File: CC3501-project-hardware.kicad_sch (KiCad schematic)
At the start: 19 parts, among them J1 USB_C_Receptacle_USB2.0_16P, J2 Conn_01x02, U1 RP2040, U2 AMS1117-3.3, U3 CR2013-MI2120, U4 DS18B20, U5 DS18B20, U6 DS18B20, U7 HX711, U8 W25Q128JVSIQTR

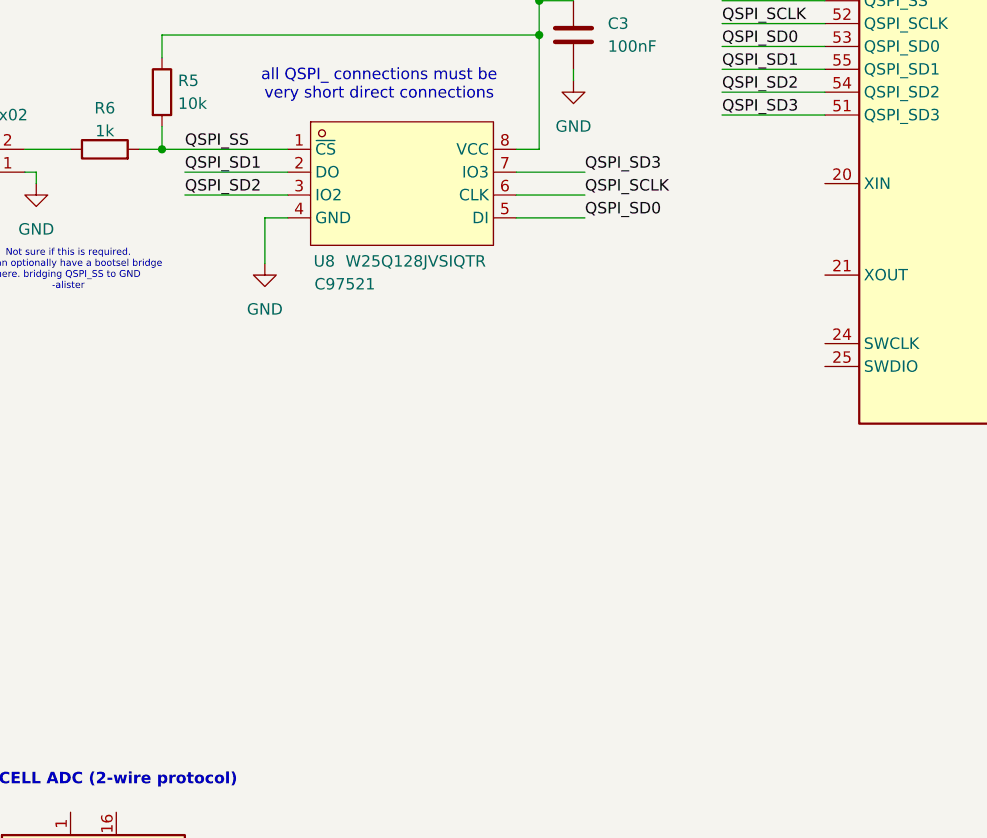
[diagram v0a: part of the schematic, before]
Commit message: Clock added
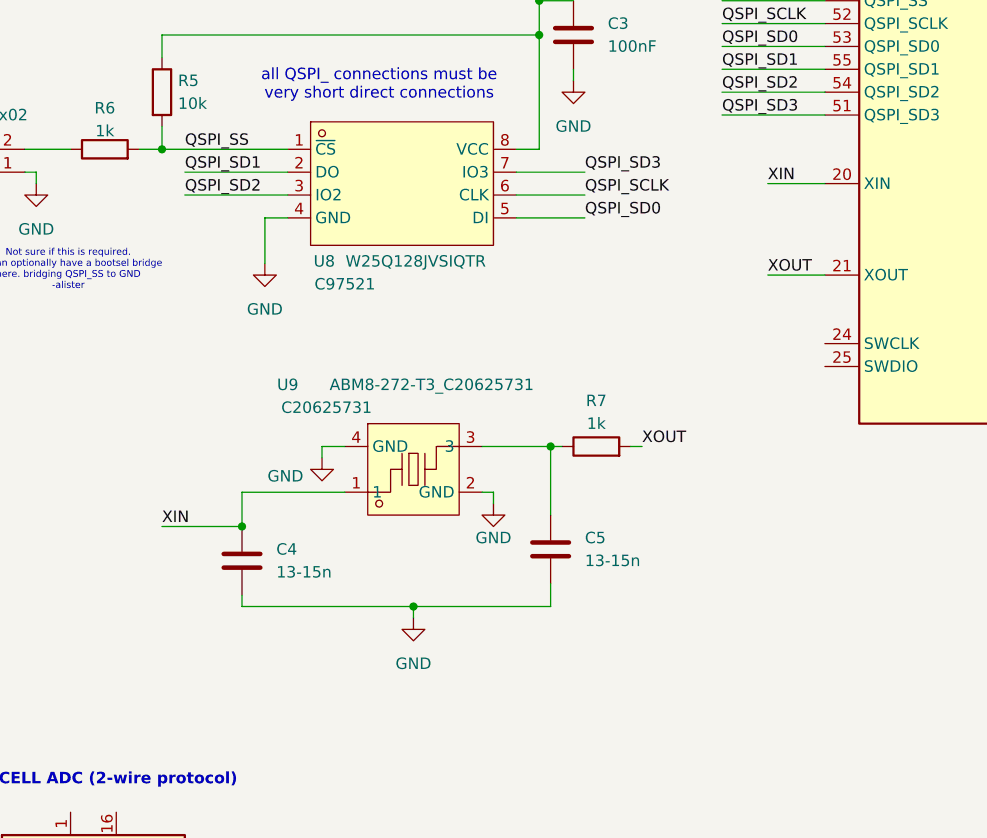
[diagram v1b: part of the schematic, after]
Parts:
- added C4, C5: 13-15n, symbol Device:C
- added R7: 1k, symbol Device:R
- added U9: ABM8-272-T3_C20625731, lcsc:CRYSTAL-SMD_4P-L3.2-W2.5-BL, symbol lcsc:ABM8-272-T3_C20625731
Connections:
- net GND: now also C4.2, C5.2, U9.2 (GND), U9.4 (GND)
- net XIN: now reaches U1.20 (XIN)
- net XIN: now also C4.1, U9.1
- net XOUT: now reaches U1.21 (XOUT)
- net XOUT: now also R7.2
- new net: C5.1, R7.1, U9.3

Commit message: Added a seperate page for rp2040 required parts
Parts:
- removed C3: 100nF, symbol Device:C
- removed C4, C5: 13-15n, symbol Device:C
- removed J2: Conn_01x02, symbol Connector_Generic:Conn_01x02
- removed R5: 10k, symbol Device:R
- removed R6, R7: 1k, symbol Device:R
- removed U8: W25Q128JVSIQTR, lcsc:SOIC-8_L5.3-W5.3-P1.27-LS8.0-BL, symbol lcsc:W25Q128JVSIQTR
- removed U9: ABM8-272-T3_C20625731, lcsc:CRYSTAL-SMD_4P-L3.2-W2.5-BL, symbol lcsc:ABM8-272-T3_C20625731
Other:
- added sheet rp2040stuff (untitled.kicad_sch)
- note removed: "Not sure if this is required. we can optionally have a bootsel bridge here. bridging QSPI_SS to GND -alister"
- note removed: "all QSPI_ connections must be very short direct connections"

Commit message: Renamed page 2
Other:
- sheet rp2040stuff renamed rp2040 components
- sheet rp2040 components: file untitled.kicad_sch -> rp2040components.kicad_sch
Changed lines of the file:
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@@
 			(color 0 0 0 0)
 		)
-		(property "Sheetname" "rp2040stuff"
+		(property "Sheetname" "rp2040 components"
 			(at 332.74 1.8284 0)
 			(show_name no)
@@
 			)
 		)
-		(property "Sheetfile" "untitled.kicad_sch"
+		(property "Sheetfile" "rp2040components.kicad_sch"
 			(at 332.74 211.4046 0)
 			(show_name no)

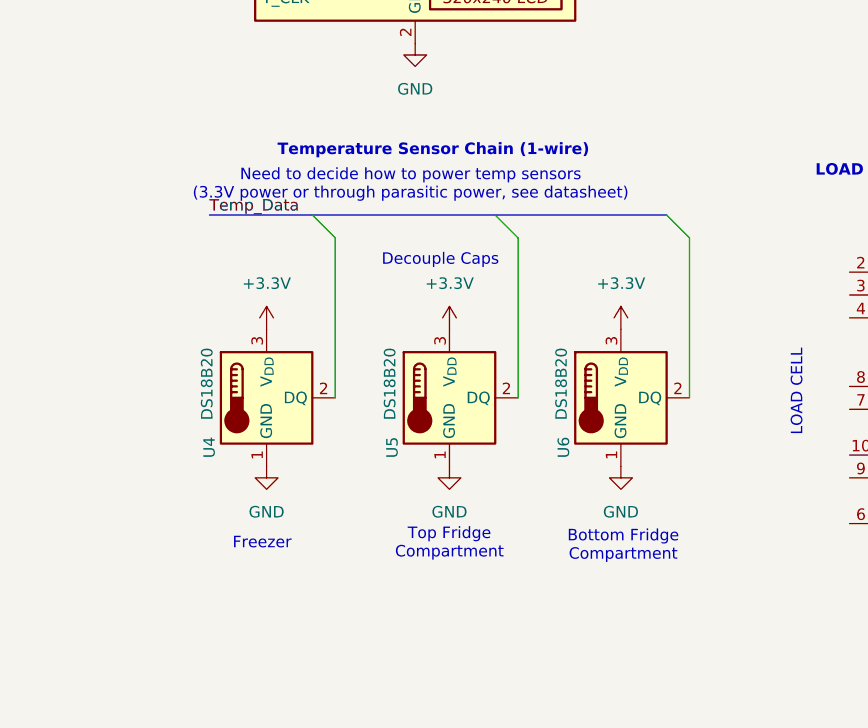
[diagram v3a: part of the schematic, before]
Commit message: Move DS18B20 breakout board into schematic.
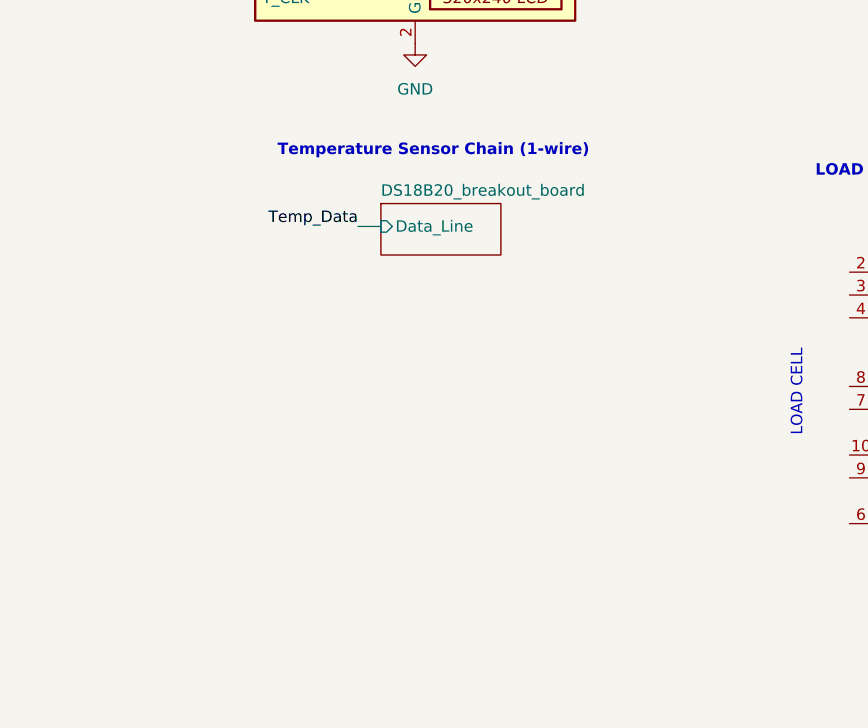
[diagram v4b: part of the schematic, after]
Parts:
- removed U4, U5, U6: DS18B20, Package_TO_SOT_THT:TO-92_Inline, symbol Sensor_Temperature:DS18B20
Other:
- added sheet DS18B20_breakout_board (DS18B20_breakout_board\DS18B20_breakout_board.kicad_sch)
- note removed: "Bottom Fridge Compartment"
- note removed: "Freezer"
- note removed: "Need to decide how to power temp sensors (3.3V power or through parasitic power, see datasheet)"
- note removed: "Top Fridge Compartment"

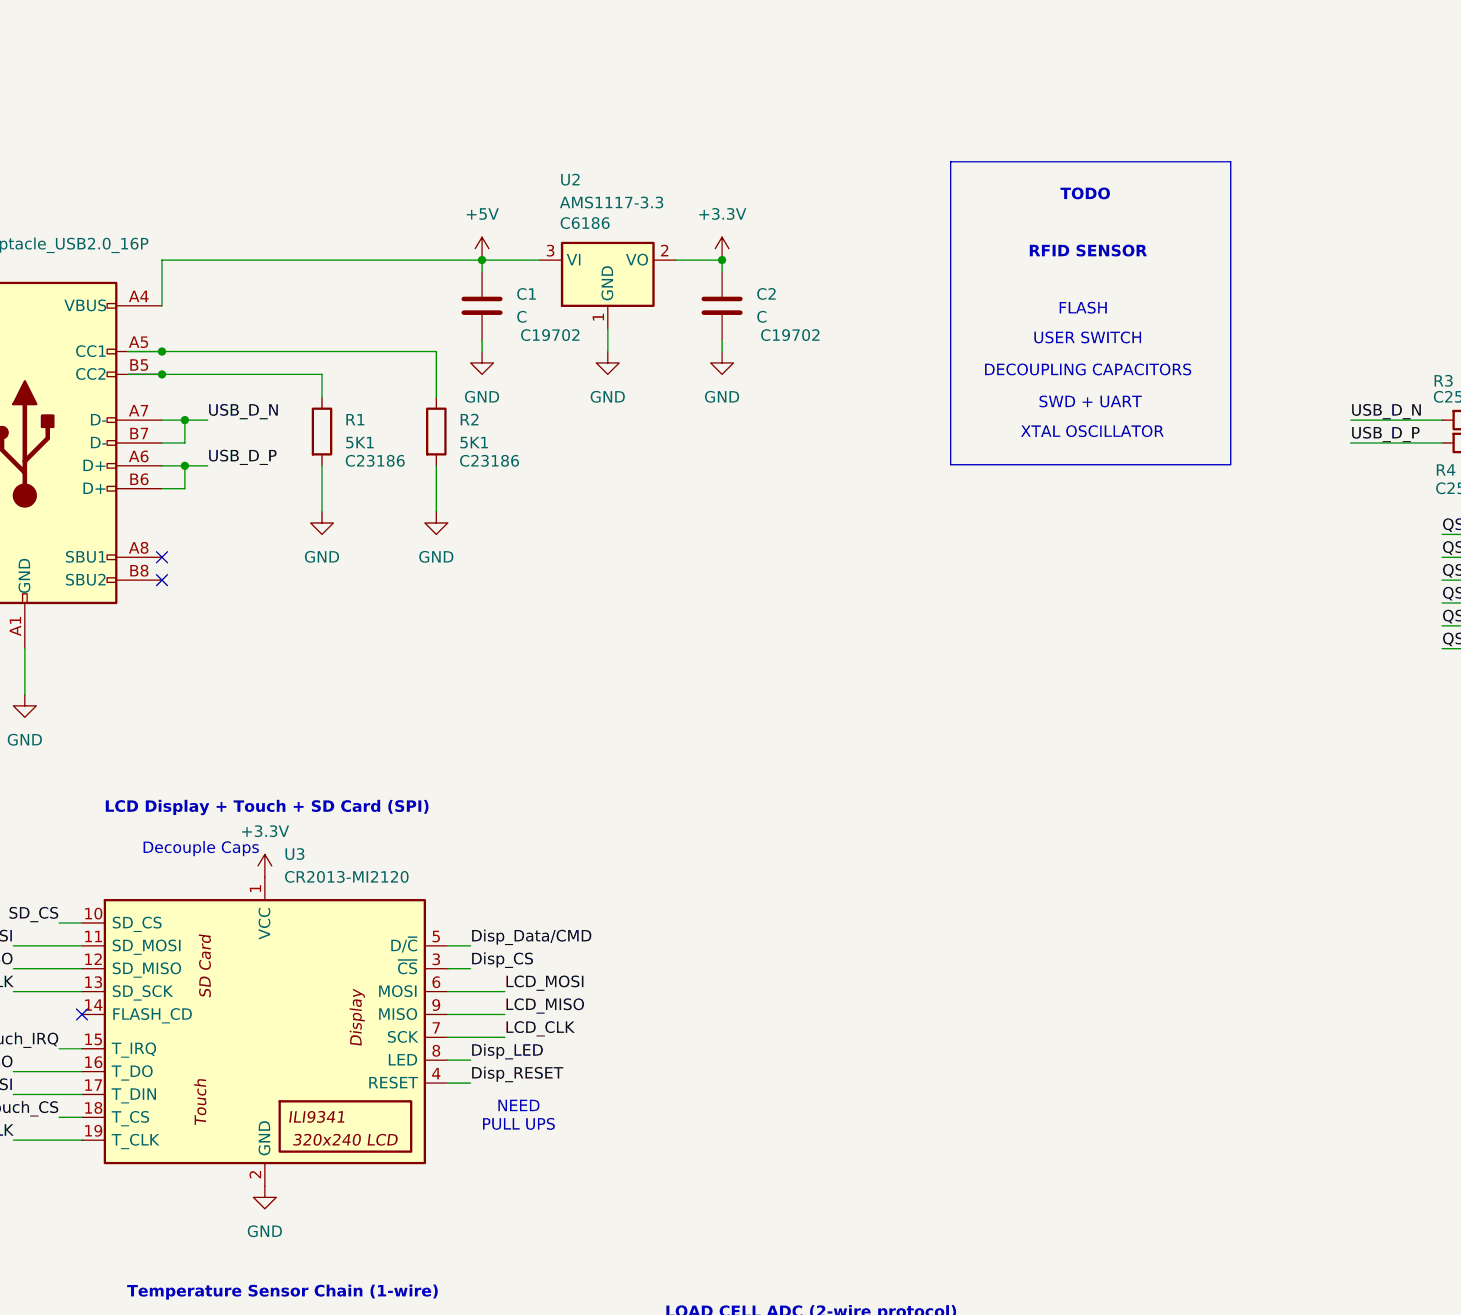
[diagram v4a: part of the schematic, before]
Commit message: add new dc-dc converter with recommended circuit layout for 3.3v
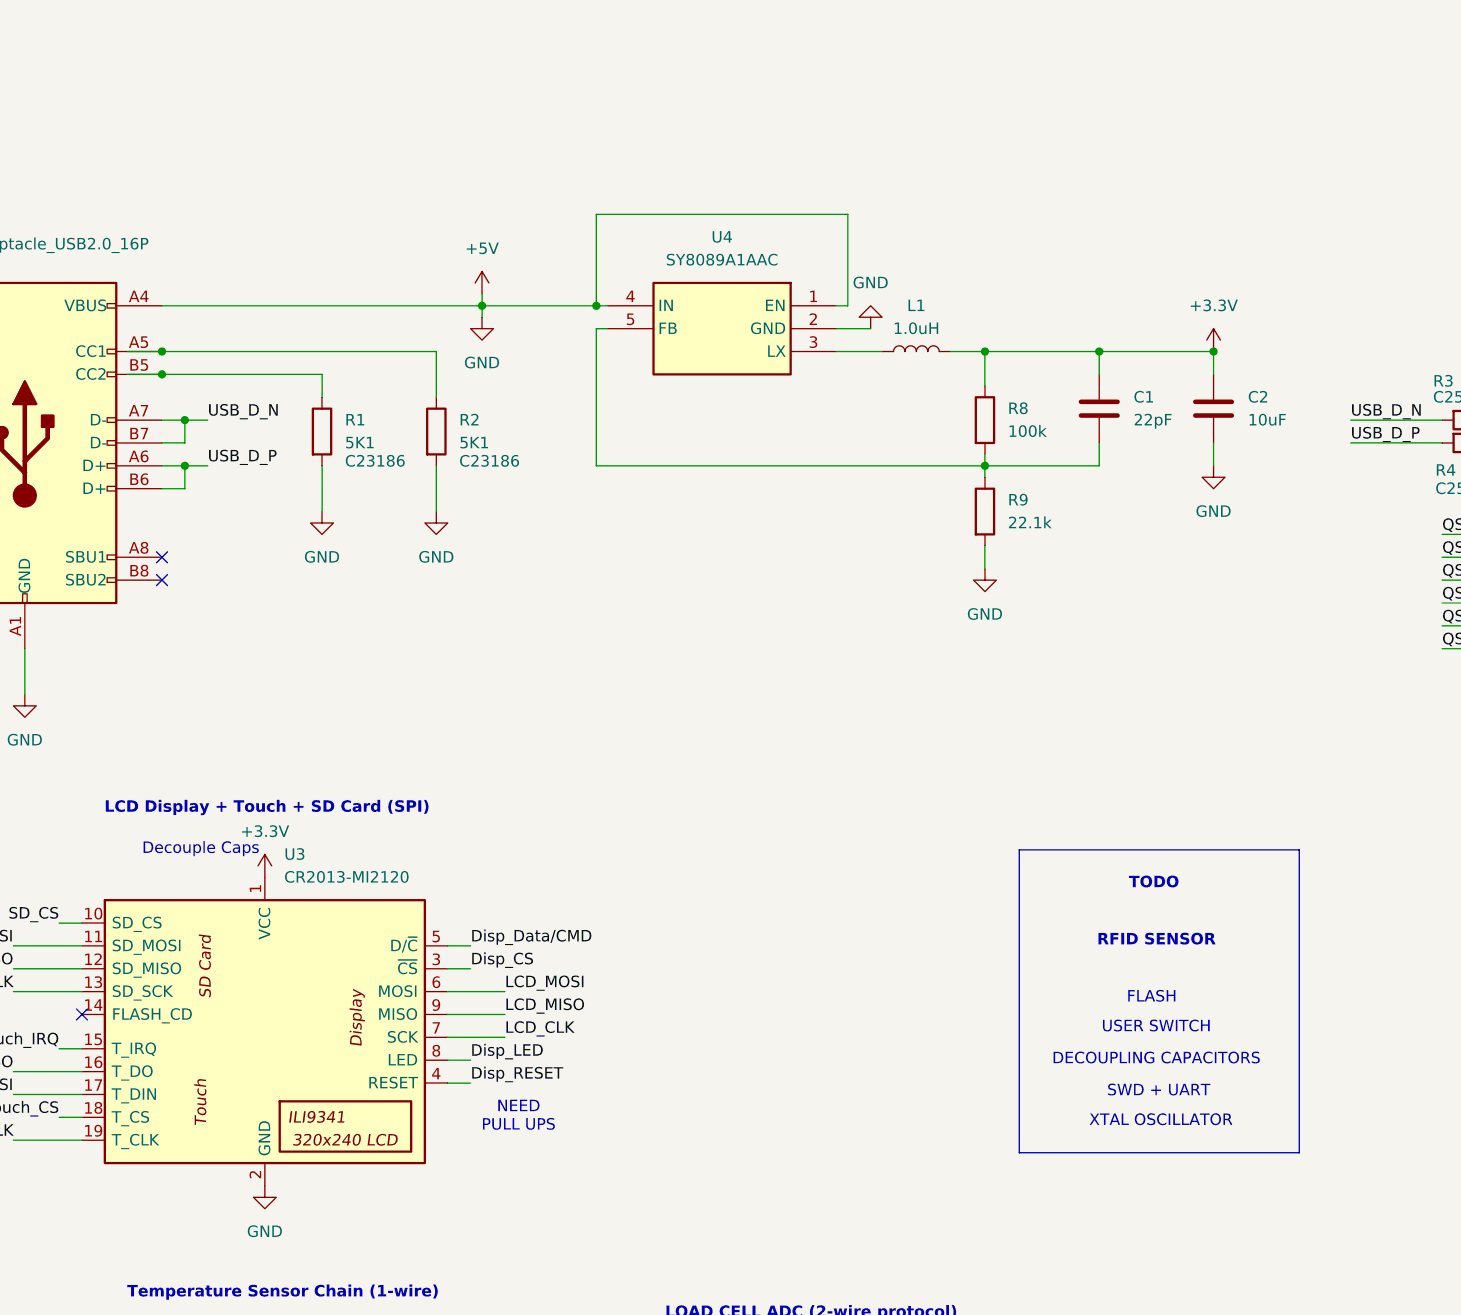
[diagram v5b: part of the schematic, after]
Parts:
- removed U2: AMS1117-3.3, Package_TO_SOT_SMD:SOT-223-3_TabPin2, symbol Regulator_Linear:AMS1117-3.3
- added L1: 1.0uH, symbol Device:L
- added R8: 100k, symbol Device:R
- added R9: 22.1k, symbol Device:R
- added U4: SY8089A1AAC, SOT95P285X130-5N, symbol SamacSys_Parts:SY8089A1AAC
- C1: value C -> 22pF; footprint Capacitor_SMD:C_0201_0603Metric -> (none); LSCS PN C19702 -> (none)
- C2: value C -> 10uF; footprint Capacitor_SMD:C_0201_0603Metric -> (none); LSCS PN C19702 -> (none)
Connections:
- net +3.3V: now also C1.1, L1.1, R8.1
- net +5V: now also C2.2, J1.A1 (GND), J1.A12 (GND), J1.B1 (GND), J1.B12 (GND), J1.SH (SHIELD), R1.2, R2.2, U3.2 (GND), R9.2, U4.1 (EN), U4.2 (GND), U4.4 (IN); no longer C1.1
- removed net GND: C1.2, C2.2, J1.A1 (GND), J1.A12 (GND), J1.B1 (GND), J1.B12 (GND), J1.SH (SHIELD), R1.2, R2.2, U3.2 (GND)
- new net: C1.2, R8.2, R9.1, U4.5 (FB)
- new net: L1.2, U4.3 (LX)
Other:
- sheet DS18B20_breakout_board: file DS18B20_breakout_board\DS18B20_breakout_board.kicad_sch -> DS18B20_breakout_board/DS18B20_breakout_board.kicad_sch

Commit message: finalise dc-dc step down.
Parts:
- added C6: 10uF, Capacitor_SMD:C_0402_1005Metric, symbol Device:C
- C1: footprint (none) -> Capacitor_SMD:C_0402_1005Metric; LCSC PN (none) -> C1555
- C2: footprint (none) -> Capacitor_SMD:C_0603_1608Metric; LCSC PN (none) -> C19702
- L1: footprint (none) -> SamacSys_Parts:IND-SMD_L4.5-W4.0; LCSC PN (none) -> C2929415
- R8: footprint (none) -> Resistor_SMD:R_0603_1608Metric; LCSC PN (none) -> C25803
- R9: footprint (none) -> Resistor_SMD:R_0603_1608Metric; LCSC PN (none) -> C31850
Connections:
- net +5V: now also C6.1, C6.2
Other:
- moved on the sheet: C1, C2, L1, R3, R4, R8, R9, U1, U4

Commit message: add temp sensor pull up fet and pull up resistor
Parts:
- added Q1: AO3400A, Package_TO_SOT_SMD:SOT-23, symbol Transistor_FET:AO3400A
- added R10: 7.4k, Resistor_SMD:R_0603_1608Metric, symbol Device:R
- added R11: 100, Resistor_SMD:R_0402_1005Metric, symbol Device:R
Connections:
- net +3.3V: now also Q1.3 (D), R10.1
- net +5V: now also U1.57 (GND)
- net Temp_Data: now also Q1.2 (S), R10.2
- net Temp_Pullup: now reaches U1.7 (GPIO5)
- net Temp_Pullup: now also R11.1
- net QSPI_SS renamed QSPI_CS
- new net: Q1.1 (G), R11.2
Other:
- sheet rp2040 components ports: added QSPI_CS, QSPI_SCLK, QSPI_SD0, QSPI_SD1, QSPI_SD2, QSPI_SD3, XIN, XOUT; removed none
